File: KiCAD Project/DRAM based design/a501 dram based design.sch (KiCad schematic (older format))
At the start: 10 parts, among them J1 Conn_02x28_Odd_Even, U1 AS7C4098A, U2 AS7C4098A

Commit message: Started work on a DRAM based design instead to keep it simple
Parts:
- removed R1: 0R, Resistors_SMD:R_0805_HandSoldering, symbol R
- removed U1, U2: AS7C4098A, Amiga_RAM:TSOP-44, symbol AS7C4098A
- removed U? (x6): iCE40-HX1K-VQ100, symbol iCE40-HX1K-VQ100
- added U? (x2): M11B416256A-35TG, Amiga_RAM:SOJ-40, symbol M11B416256A-35TG
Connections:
- wire segments 97 -> 91
- no-connect marks 3 -> 5
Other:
- note removed: "Don't populate\nresistor"

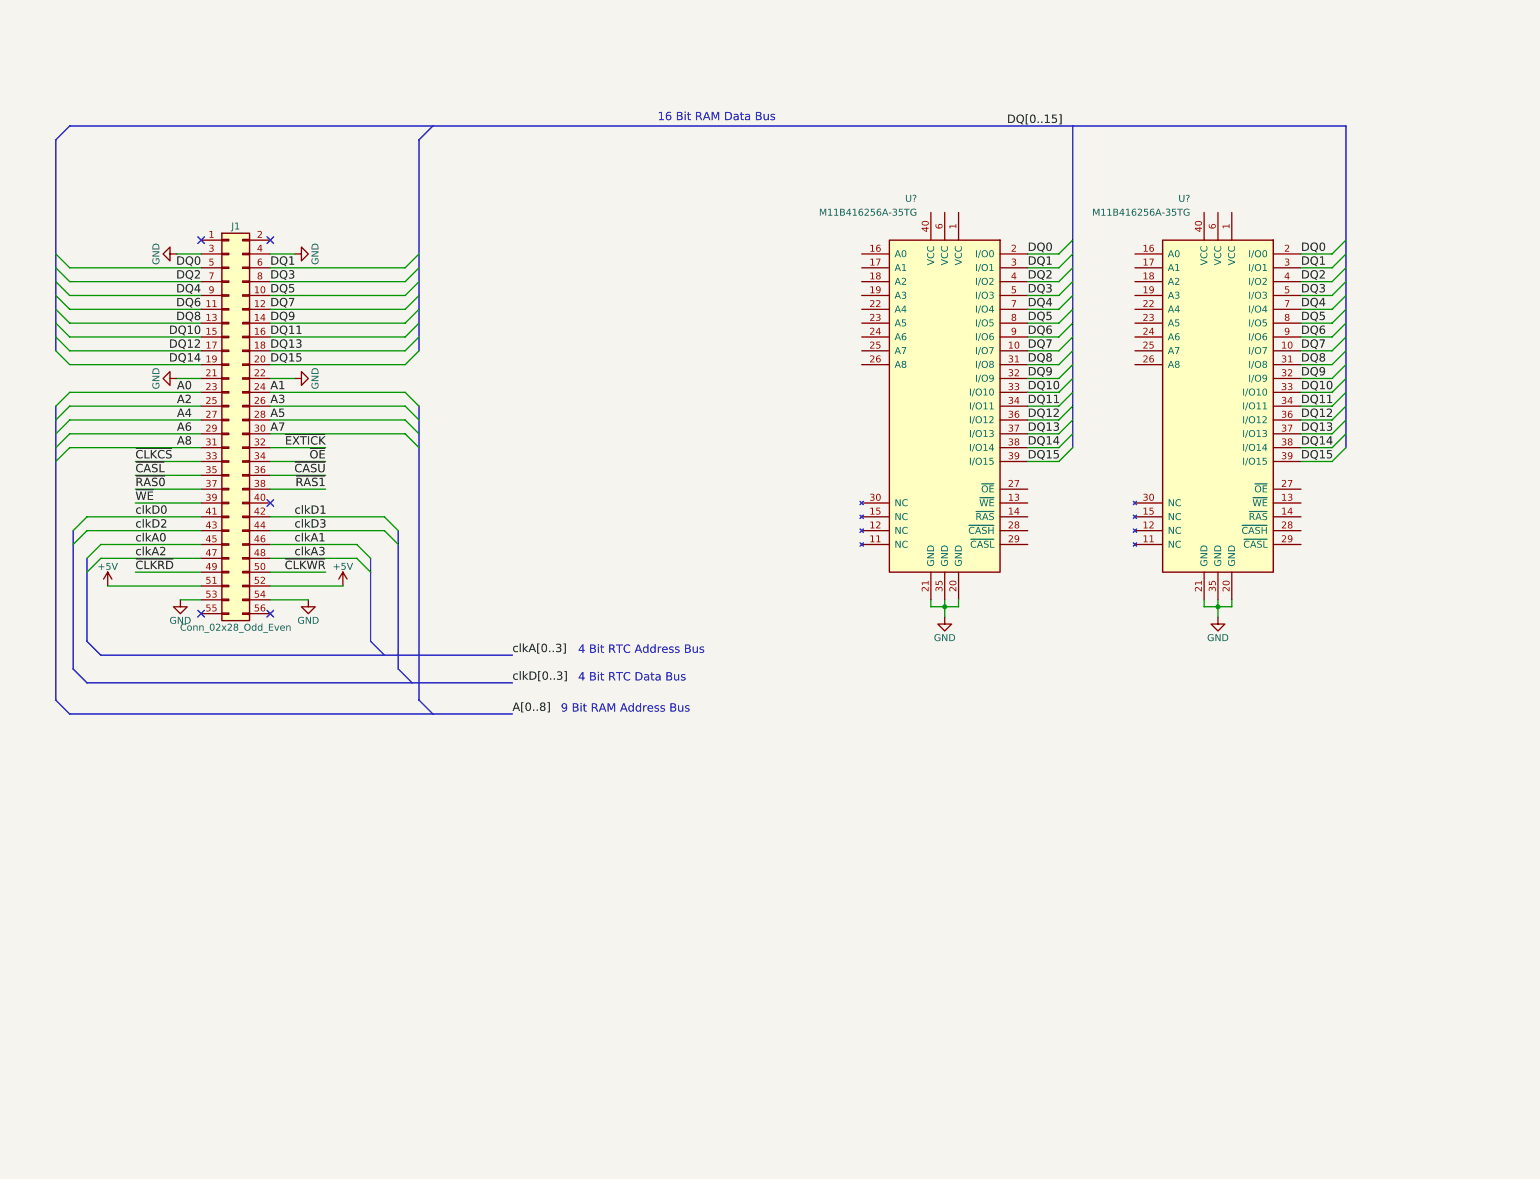
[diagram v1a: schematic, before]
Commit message: Completed DRAM expansion design
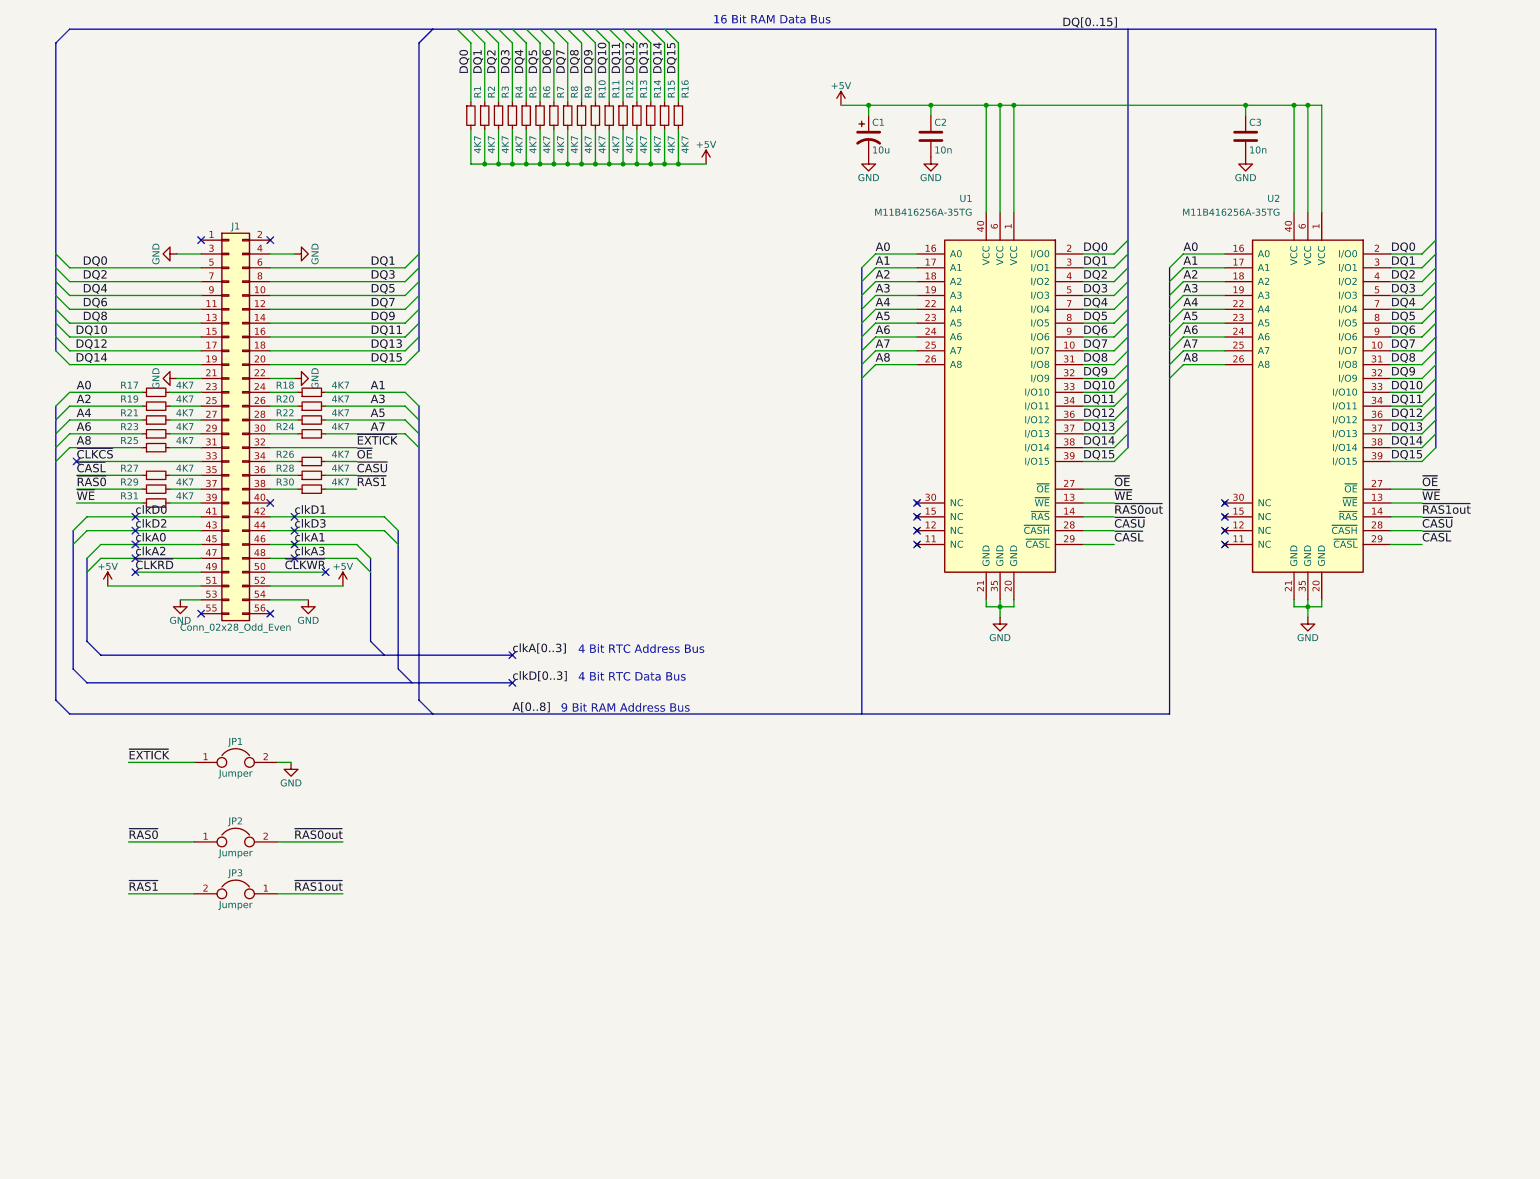
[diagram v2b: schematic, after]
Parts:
- added C1: 10u, Capacitors_SMD:C_0805_HandSoldering, symbol CP1
- added C2, C3: 10n, Capacitors_SMD:C_0805_HandSoldering, symbol C
- added JP1, JP2, JP3: Jumper, Pin_Headers:Pin_Header_Straight_1x02_Pitch2.54mm, symbol Jumper
- added R1, R10, R11, R12, R13, R14, R15, R16, R17, R18, R19, R2, R20, R21, R22, R23, R24, R25, R26, R27, R28, R29, R3, R30, R31, R4, R5, R6, R7, R8, R9: 4K7, Resistors_SMD:R_0805_HandSoldering, symbol R_Small
- J1: footprint Pin_Headers:Pin_Header_Angled_2x28_Pitch2.54mm -> Amiga_RAM:Pin_Header_Angled_Female_2x28_Pitch2.54mm
- gave numbers to parts that had none: 2
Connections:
- net +5V: now also U1.1 (VCC), U1.40 (VCC), U1.6 (VCC), U2.1 (VCC), U2.40 (VCC), U2.6 (VCC), C1.1, C2.1, C3.1, R1.2, R10.2, R11.2, R12.2, R13.2, R14.2, R15.2, R16.2, R2.2, R3.2, R4.2, R5.2, R6.2, R7.2, R8.2, R9.2
- net A0: now also U1.16 (A0), U2.16 (A0), R17.1; no longer J1.23 (Pin_23)
- net A1: now also U1.17 (A1), U2.17 (A1), R18.2; no longer J1.24 (Pin_24)
- net A2: now also U1.18 (A2), U2.18 (A2), R19.1; no longer J1.25 (Pin_25)
- net A3: now also U1.19 (A3), U2.19 (A3), R20.2; no longer J1.26 (Pin_26)
- net A4: now also U1.22 (A4), U2.22 (A4), R21.1; no longer J1.27 (Pin_27)
- net A5: now also U1.23 (A5), U2.23 (A5), R22.2; no longer J1.28 (Pin_28)
- net A6: now also U1.24 (A6), U2.24 (A6), R23.1; no longer J1.29 (Pin_29)
- net A7: now also U1.25 (A7), U2.25 (A7), R24.2; no longer J1.30 (Pin_30)
- net A8: now also U1.26 (A8), U2.26 (A8), R25.1; no longer J1.31 (Pin_31)
- net DQ0: now also R1.1
- net DQ1: now also R2.1
- net DQ10: now also R11.1
- net DQ11: now also R12.1
- net DQ12: now also R13.1
- net DQ13: now also R14.1
- net DQ14: now also R15.1
- net DQ15: now also R16.1
- net DQ2: now also R3.1
- net DQ3: now also R4.1
- net DQ4: now also R5.1
- net DQ5: now also R6.1
- net DQ6: now also R7.1
- net DQ7: now also R8.1
- net DQ8: now also R9.1
- net DQ9: now also R10.1
- net GND: now also C1.2, C2.2, C3.2, JP1.2
- net ~CASL: now also U1.29 (~CASL), U2.29 (~CASL), R27.1; no longer J1.35 (Pin_35)
- net ~CASU: now also U1.28 (~CASH), U2.28 (~CASH), R28.2; no longer J1.36 (Pin_36)
- net ~EXTICK: now also JP1.1
- net ~OE: now also U1.27 (~OE), U2.27 (~OE), R26.2; no longer J1.34 (Pin_34)
- net ~RAS0: now also JP2.1, R29.1; no longer J1.37 (Pin_37)
- net ~RAS1: now also JP3.2, R30.2; no longer J1.38 (Pin_38)
- net ~WE: now also U1.13 (~WE), U2.13 (~WE), R31.1; no longer J1.39 (Pin_39)
- net ~RAS0out: now reaches U1.14 (~RAS)
- net ~RAS0out: now also JP2.2
- net ~RAS1out: now reaches U2.14 (~RAS)
- net ~RAS1out: now also JP3.1
- new net: J1.23 (Pin_23), R17.2
- new net: J1.24 (Pin_24), R18.1
- new net: J1.25 (Pin_25), R19.2
- new net: J1.26 (Pin_26), R20.1
- new net: J1.27 (Pin_27), R21.2
- new net: J1.28 (Pin_28), R22.1
- new net: J1.29 (Pin_29), R23.2
- new net: J1.30 (Pin_30), R24.1
- new net: J1.31 (Pin_31), R25.2
- new net: J1.34 (Pin_34), R26.1
- new net: J1.35 (Pin_35), R27.2
- new net: J1.36 (Pin_36), R28.1
- new net: J1.37 (Pin_37), R29.2
- new net: J1.38 (Pin_38), R30.1
- new net: J1.39 (Pin_39), R31.2
- no-connect marks 5 -> 26
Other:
- moved on the sheet: U1, U2

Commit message: Adding the completed keypad prototype kicad files. Finished a long time ago, just forgot to push
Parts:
- removed R1, R10, R11, R12, R13, R14, R15, R16, R2, R3, R4, R5, R6, R7, R8, R9: 4K7, Resistors_SMD:R_0805_HandSoldering, symbol R_Small
- added C3, C5: 10n, Capacitor_SMD:C_0805_2012Metric_Pad1.15x1.40mm_HandSolder, symbol a501-dram-based-design-rescue:C
- added C4: 10u, Capacitor_SMD:C_0805_2012Metric_Pad1.15x1.40mm_HandSolder, symbol a501-dram-based-design-rescue:CP1
- C1: footprint Capacitors_SMD:C_0805_HandSoldering -> Capacitor_SMD:C_0805_2012Metric_Pad1.15x1.40mm_HandSolder; symbol CP1 -> a501-dram-based-design-rescue:CP1
- C2: footprint Capacitors_SMD:C_0805_HandSoldering -> Capacitor_SMD:C_0805_2012Metric_Pad1.15x1.40mm_HandSolder; symbol C -> a501-dram-based-design-rescue:C
- C6: renamed from C3; footprint Capacitors_SMD:C_0805_HandSoldering -> Capacitor_SMD:C_0805_2012Metric_Pad1.15x1.40mm_HandSolder; symbol C -> a501-dram-based-design-rescue:C
- J1: symbol Conn_02x28_Odd_Even -> a501-dram-based-design-rescue:Conn_02x28_Odd_Even
- JP1, JP2, JP3: symbol Jumper -> a501-dram-based-design-rescue:Jumper
- R1: renamed from R17; footprint Resistors_SMD:R_0805_HandSoldering -> Resistor_SMD:R_0805_2012Metric_Pad1.15x1.40mm_HandSolder; symbol R_Small -> a501-dram-based-design-rescue:R_Small
- R10: renamed from R20; footprint Resistors_SMD:R_0805_HandSoldering -> Resistor_SMD:R_0805_2012Metric_Pad1.15x1.40mm_HandSolder; symbol R_Small -> a501-dram-based-design-rescue:R_Small
- R11: renamed from R22; footprint Resistors_SMD:R_0805_HandSoldering -> Resistor_SMD:R_0805_2012Metric_Pad1.15x1.40mm_HandSolder; symbol R_Small -> a501-dram-based-design-rescue:R_Small
- R12: renamed from R24; footprint Resistors_SMD:R_0805_HandSoldering -> Resistor_SMD:R_0805_2012Metric_Pad1.15x1.40mm_HandSolder; symbol R_Small -> a501-dram-based-design-rescue:R_Small
- R13: renamed from R26; footprint Resistors_SMD:R_0805_HandSoldering -> Resistor_SMD:R_0805_2012Metric_Pad1.15x1.40mm_HandSolder; symbol R_Small -> a501-dram-based-design-rescue:R_Small
- R14: renamed from R28; footprint Resistors_SMD:R_0805_HandSoldering -> Resistor_SMD:R_0805_2012Metric_Pad1.15x1.40mm_HandSolder; symbol R_Small -> a501-dram-based-design-rescue:R_Small
- R15: renamed from R30; footprint Resistors_SMD:R_0805_HandSoldering -> Resistor_SMD:R_0805_2012Metric_Pad1.15x1.40mm_HandSolder; symbol R_Small -> a501-dram-based-design-rescue:R_Small
- R2: renamed from R19; footprint Resistors_SMD:R_0805_HandSoldering -> Resistor_SMD:R_0805_2012Metric_Pad1.15x1.40mm_HandSolder; symbol R_Small -> a501-dram-based-design-rescue:R_Small
- R3: renamed from R21; footprint Resistors_SMD:R_0805_HandSoldering -> Resistor_SMD:R_0805_2012Metric_Pad1.15x1.40mm_HandSolder; symbol R_Small -> a501-dram-based-design-rescue:R_Small
- R4: renamed from R23; footprint Resistors_SMD:R_0805_HandSoldering -> Resistor_SMD:R_0805_2012Metric_Pad1.15x1.40mm_HandSolder; symbol R_Small -> a501-dram-based-design-rescue:R_Small
- R5: renamed from R25; footprint Resistors_SMD:R_0805_HandSoldering -> Resistor_SMD:R_0805_2012Metric_Pad1.15x1.40mm_HandSolder; symbol R_Small -> a501-dram-based-design-rescue:R_Small
- R6: renamed from R27; footprint Resistors_SMD:R_0805_HandSoldering -> Resistor_SMD:R_0805_2012Metric_Pad1.15x1.40mm_HandSolder; symbol R_Small -> a501-dram-based-design-rescue:R_Small
- R7: renamed from R29; footprint Resistors_SMD:R_0805_HandSoldering -> Resistor_SMD:R_0805_2012Metric_Pad1.15x1.40mm_HandSolder; symbol R_Small -> a501-dram-based-design-rescue:R_Small
- R8: renamed from R31; footprint Resistors_SMD:R_0805_HandSoldering -> Resistor_SMD:R_0805_2012Metric_Pad1.15x1.40mm_HandSolder; symbol R_Small -> a501-dram-based-design-rescue:R_Small
- R9: renamed from R18; footprint Resistors_SMD:R_0805_HandSoldering -> Resistor_SMD:R_0805_2012Metric_Pad1.15x1.40mm_HandSolder; symbol R_Small -> a501-dram-based-design-rescue:R_Small
- U1, U2: symbol M11B416256A-35TG -> AmigaRAM:M11B416256A-35TG
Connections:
- net +5V: now also U1.20 (VCC), U2.20 (VCC), C3.1, C4.1, C5.1; no longer U1.40 (VCC), U2.40 (VCC)
- net GND: now also U1.40 (GND), U2.40 (GND), C3.2, C4.2, C5.2; no longer U1.20 (GND), U2.20 (GND)
- net ~RAS0: now also J1.37 (Pin_37); no longer R7.1
- net ~RAS0out: now also R7.2; no longer JP2.2
- net ~RAS1: now also J1.38 (Pin_38); no longer R15.2
- net ~RAS1out: now also R15.2; no longer JP3.1
- net at R15.1: now also JP3.1; no longer J1.38 (Pin_38)
- new net: JP2.2, R7.1
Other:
- moved on the sheet: C1, C2, C6, J1, JP1, JP2, JP3, R1, R10, R11, R12, R13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
